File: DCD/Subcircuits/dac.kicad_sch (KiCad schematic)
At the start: 25 parts, among them U10 OPA277UA, U11 DAC8811ICDGKT, U12 DAC8811ICDGKT, U13 OPA277UA, U14 OPA277UA

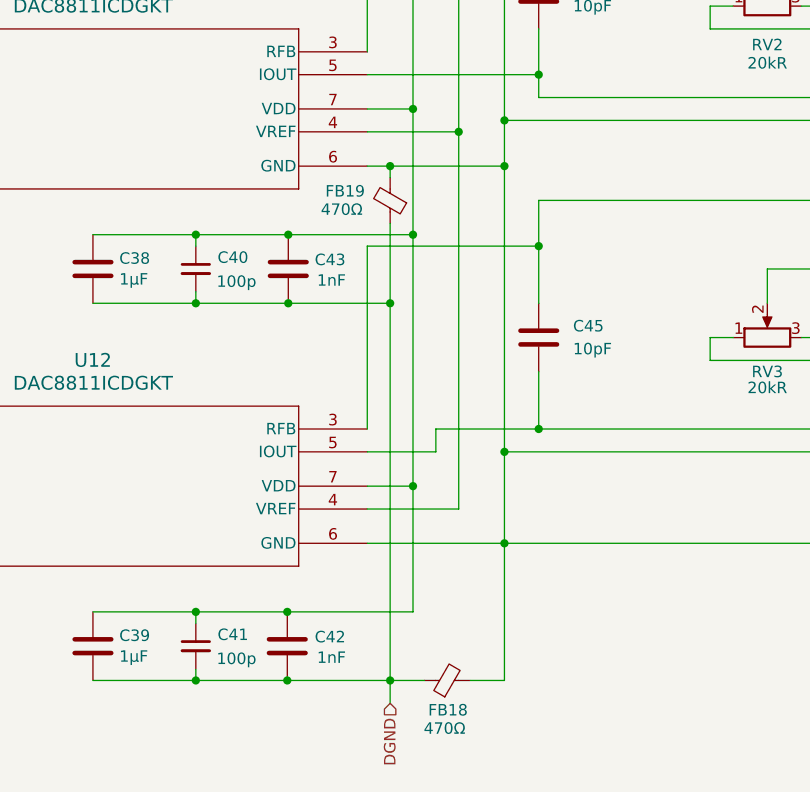
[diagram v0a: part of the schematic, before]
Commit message: Finished the layout
Modified ground planes separation, finished stiching, fixed drc errors
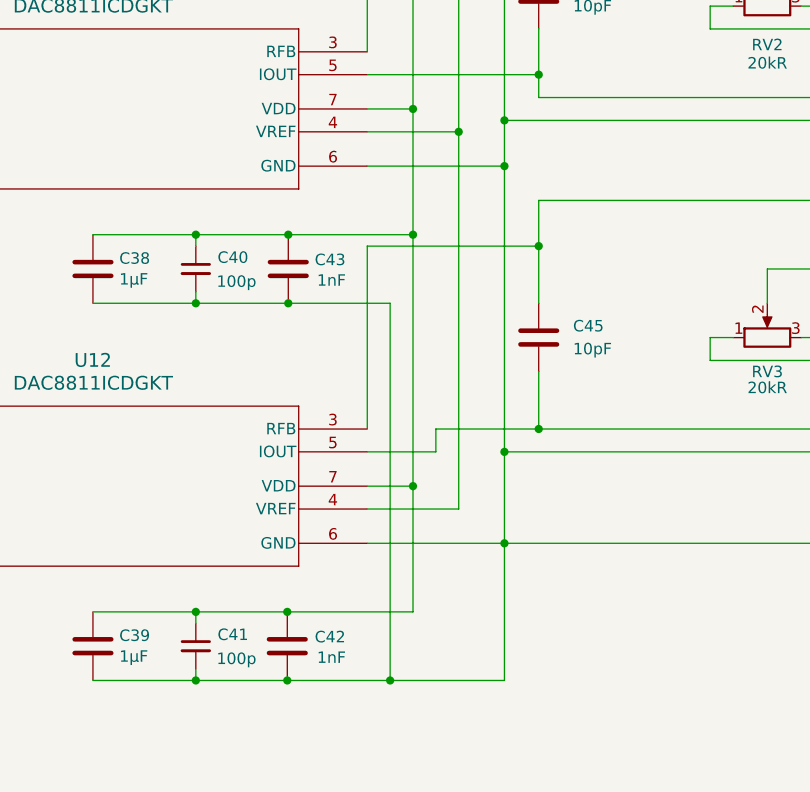
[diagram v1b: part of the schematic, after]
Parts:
- removed FB18, FB19: 470Ω, Inductor_SMD:L_0603_1608Metric, symbol Device:FerriteBead_Small
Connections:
- net DGND is gone; now on net AGND: C38.2, C39.2, C40.2, C41.2, C42.2, C43.2

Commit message: added part numbers
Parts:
- U10, U14: Link (none) -> https://nl.mouser.com/ProductDetail/Texas-Instruments/OPA27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; Order number (none) -> 595-OPA277UA; Part number (none) -> OPA277UA; Supplier (none) -> Mouser
- U11, U12: Link (none) -> https://nl.mouser.com/ProductDetail/Texas-Instruments/DAC88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; Order number (none) -> 595-DAC8811ICDGKT; Part number (none) -> DAC8811ICDGKT; Supplier (none) -> Mouser
- U13: Link (none) -> https://nl.mouser.com/ProductDetail/Texas-Instruments/OPA27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; Order  number (none) -> 595-OPA277UA; Part number (none) -> OPA277UA; Supplier (none) -> Mouser
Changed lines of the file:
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@@
+			)
+		)
+		(property "Part number" "DAC8811ICDGKT"
+			(at 49.53 128.27 0)
+			(effects
+				(font
+					(size 1.27 1.27)
+				)
+				(hide yes)
+			)
+		)
+		(property "Order number" "595-DAC8811ICDGKT"
+			(at 49.53 128.27 0)
+			(effects
+				(font
+					(size 1.27 1.27)
+				)
+				(hide yes)
+			)
+		)
+		(property "Supplier" "Mouser"
+			(at 49.53 128.27 0)
+			(effects
+				(font
+					(size 1.27 1.27)
+				)
+				(hide yes)
+			)
+		)
+		(property "Link" "https://nl.mouser.com/ProductDetail/Texas-Instruments/DAC8811ICDGKT?qs=vul0MlC%2Fa1ckja9SywYDlQ%3D%3D"
+			(at 49.53 128.27 0)
+			(effects
+				(font
+					(size 1.27 1.27)
+				)
+				(hide yes)
 			)
 		)
@@
 			)
 		)
+		(property "Part number" "DAC8811ICDGKT"
+			(at 49.53 86.36 0)
+			(effects
+				(font
+					(size 1.27 1.27)
+				)
+				(hide yes)
+			)
+		)
+		(property "Order number" "595-DAC8811ICDGKT"
+			(at 49.53 86.36 0)
+			(effects
+				(font
+					(size 1.27 1.27)
+				)
+				(hide yes)
+			)
+		)
+		(property "Supplier" "Mouser"
+			(at 49.53 86.36 0)
+			(effects
+				(font
+					(size 1.27 1.27)
+				)
+				(hide yes)
+			)
+		)
+		(property "Link" "https://nl.mouser.com/ProductDetail/Texas-Instruments/DAC8811ICDGKT?qs=vul0MlC%2Fa1ckja9SywYDlQ%3D%3D"
+			(at 49.53 86.36 0)
+			(effects
+				(font
+					(size 1.27 1.27)
+				)
+				(hide yes)
+			)
+		)
 		(pin "1"
 		)
@@
 			)
 		)
+		(property "Part number" "OPA277UA "
+			(at 161.29 118.11 0)
+			(effects
+				(font
+					(size 1.27 1.27)
+				)
+				(hide yes)
+			)
+		)
+		(property "Order number" "595-OPA277UA"
+			(at 161.29 118.11 0)
+			(effects
+				(font
+					(size 1.27 1.27)
+				)
+				(hide yes)
+			)
+		)
+		(property "Supplier" "Mouser"
+			(at 161.29 118.11 0)
+			(effects
+				(font
+					(size 1.27 1.27)
+				)
+				(hide yes)
+			)
+		)
+		(property "Link" "https://nl.mouser.com/ProductDetail/Texas-Instruments/OPA277UA?qs=7nS3%252BbEUL6skPbgHbWHhXQ%3D%3D&srsltid=AfmBOooMYEOoq7PaAeOD3PNNu6OchYXQ-UuVUDJUEDdGbaQFtKnOjA8d"
+			(at 161.29 118.11 0)
+			(effects
+				(font
+					(size 1.27 1.27)
+				)
+				(hide yes)
+			)
+		)
 		(pin "1"
 		)
@@
 			)
 		)
+		(property "Part number" "OPA277UA "
+			(at 33.02 41.91 0)
+			(effects
+				(font
+					(size 1.27 1.27)
+				)
+				(hide yes)
+			)
+		)
+		(property "Order number" "595-OPA277UA"
+			(at 33.02 41.91 0)
+			(effects
+				(font
+					(size 1.27 1.27)
+				)
+				(hide yes)
+			)
+		)
+		(property "Supplier" "Mouser"
+			(at 33.02 41.91 0)
+			(effects
+				(font
+					(size 1.27 1.27)
+				)
+				(hide yes)
+			)
+		)
+		(property "Link" "https://nl.mouser.com/ProductDetail/Texas-Instruments/OPA277UA?qs=7nS3%252BbEUL6skPbgHbWHhXQ%3D%3D&srsltid=AfmBOooMYEOoq7PaAeOD3PNNu6OchYXQ-UuVUDJUEDdGbaQFtKnOjA8d"
+			(at 33.02 41.91 0)
+			(effects
+				(font
+					(size 1.27 1.27)
+				)
+				(hide yes)
+			)
+		)
 		(pin "1"
 		)
@@
 			(at 161.29 81.28 0)
 			(effects
+				(font
+					(size 1.27 1.27)
+				)
+				(hide yes)
+			)
+		)
+		(property "Part number" "OPA277UA "
+			(at 161.29 81.28 0)
+			(effects
+				(font
+					(size 1.27 1.27)
+				)
+				(hide yes)
+			)
+		)
+		(property "Order  number" "595-OPA277UA"
+			(at 161.29 81.28 0)
+			(effects
+				(font
+					(size 1.27 1.27)
+				)
+				(hide yes)
+			)
+		)
+		(property "Supplier" "Mouser"
+			(at 161.29 81.28 0)
+			(effects
+				(font
+					(size 1.27 1.27)
+				)
+				(hide yes)
+			)
+		)
+		(property "Link" "https://nl.mouser.com/ProductDetail/Texas-Instruments/OPA277UA?qs=7nS3%252BbEUL6skPbgHbWHhXQ%3D%3D&srsltid=AfmBOooMYEOoq7PaAeOD3PNNu6OchYXQ-UuVUDJUEDdGbaQFtKnOjA8d"
+			(at 161.29 81.28 0)
+			(effects
